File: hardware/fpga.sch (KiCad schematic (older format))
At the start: 39 parts, among them J801 Conn_02x06_Counter_Clockwise, J802 Conn_02x06_Counter_Clockwise, U801 74HC244, U802 74HC244, U803 74xx1G14

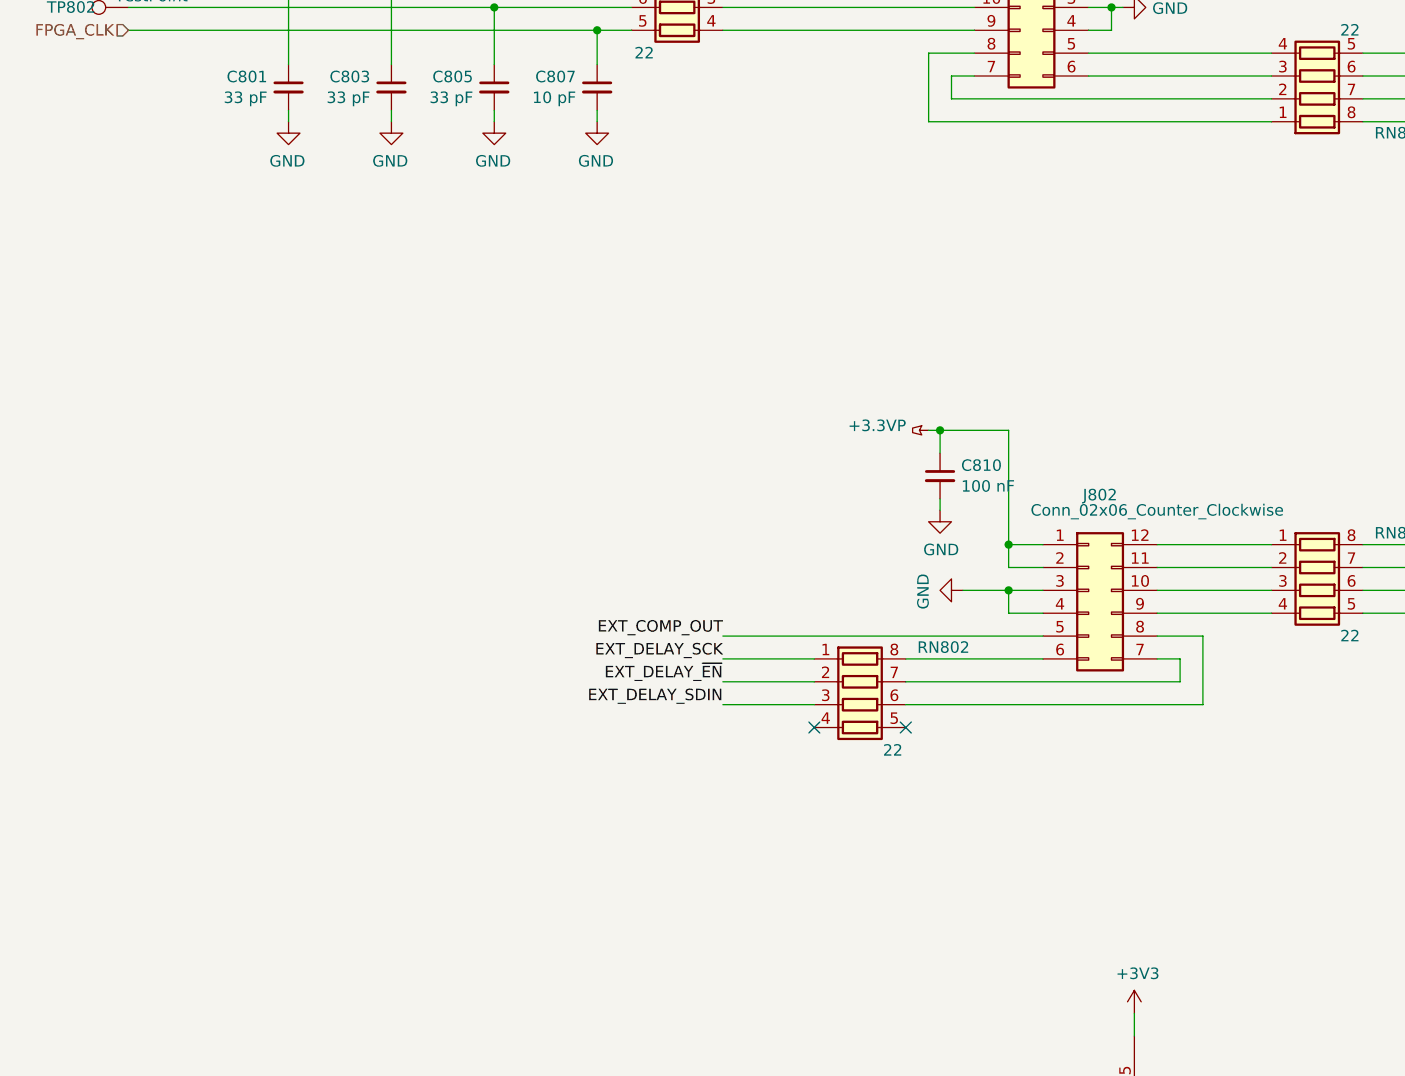
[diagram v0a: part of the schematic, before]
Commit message: improve PMOD connector pin labels in schematic..
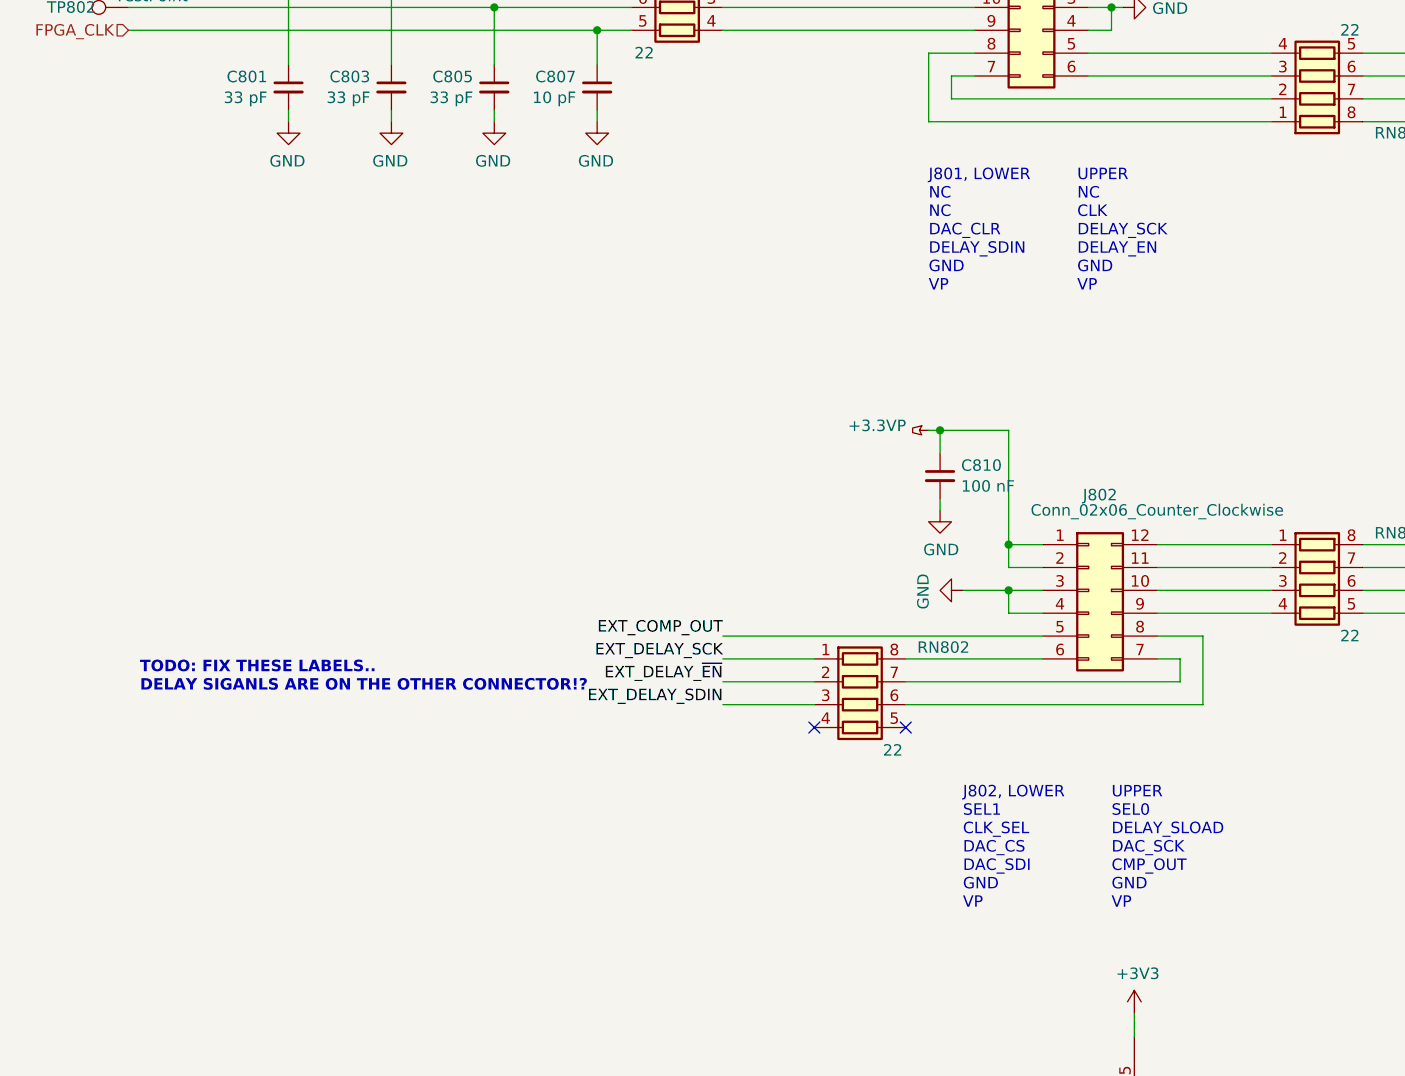
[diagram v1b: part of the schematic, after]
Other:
- note added: "J801, LOWER\nNC\nNC\nDAC_CLR\nDELAY_SDIN\nGND\nVP"
- note added: "J802, LOWER\nSEL1\nCLK_SEL\nDAC_CS\nDAC_SDI\nGND\nVP"
- note added: "TODO: FIX THESE LABELS..\nDELAY SIGANLS ARE ON THE OTHER CONNECTOR!?"
- note added: "UPPER\nNC\nCLK\nDELAY_SCK\nDELAY_EN\nGND\nVP"
- note added: "UPPER\nSEL0\nDELAY_SLOAD\nDAC_SCK\nCMP_OUT\nGND\nVP"
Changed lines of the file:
@@
 Wire Wire Line
 	1300 1850 2000 1850
+Text Notes 4800 3300 0    50   ~ 0
+J801, LOWER\nNC\nNC\nDAC_CLR\nDELAY_SDIN\nGND\nVP
+Text Notes 5450 3300 0    50   ~ 0
+UPPER\nNC\nCLK\nDELAY_SCK\nDELAY_EN\nGND\nVP
+Text Notes 4950 6000 0    50   ~ 0
+J802, LOWER\nSEL1\nCLK_SEL\nDAC_CS\nDAC_SDI\nGND\nVP
+Text Notes 5600 6000 0    50   ~ 0
+UPPER\nSEL0\nDELAY_SLOAD\nDAC_SCK\nCMP_OUT\nGND\nVP
+Text Notes 1350 5050 0    50   ~ 10
+TODO: FIX THESE LABELS..\nDELAY SIGANLS ARE ON THE OTHER CONNECTOR!?
 $EndSCHEMATC
